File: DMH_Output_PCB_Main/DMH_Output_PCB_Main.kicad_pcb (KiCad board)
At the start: 2 copper layers, 49 x 175 mm, 91 parts, among them J0 Conn_01x01, J1 TRS_Jack_6.35mm_Sw, J100 IDC_02x05, J2 TRS_Jack_6.35mm_Sw, J200 IDC_02x05, J23 Conn_01x06, J24 Conn_01x02, J25 Conn_01x02, J26 Conn_01x06_PinHeader, J27 Conn_01x06_PinHeader, J28 Conn_01x06, J29 Conn_01x04_PinHeader, J3 TRS_Jack_6.35mm_Sw, J31 Conn_01x06_PinHeader, J35 Conn_01x04_PinHeader, J4 TRS_Jack_6.35mm_Sw, J5 TRS_Jack_6.35mm_Sw, J6 TRS_Jack_6.35mm_Sw, J7 TRS_Jack_6.35mm_Sw, J8 TRS_Jack_6.35mm_Sw, J9 TRS_Jack_6.35mm_Sw, U1 TL072, U11 TL074, U13 NE5532, U15 NE5532, U20 TL072, U8 TL074

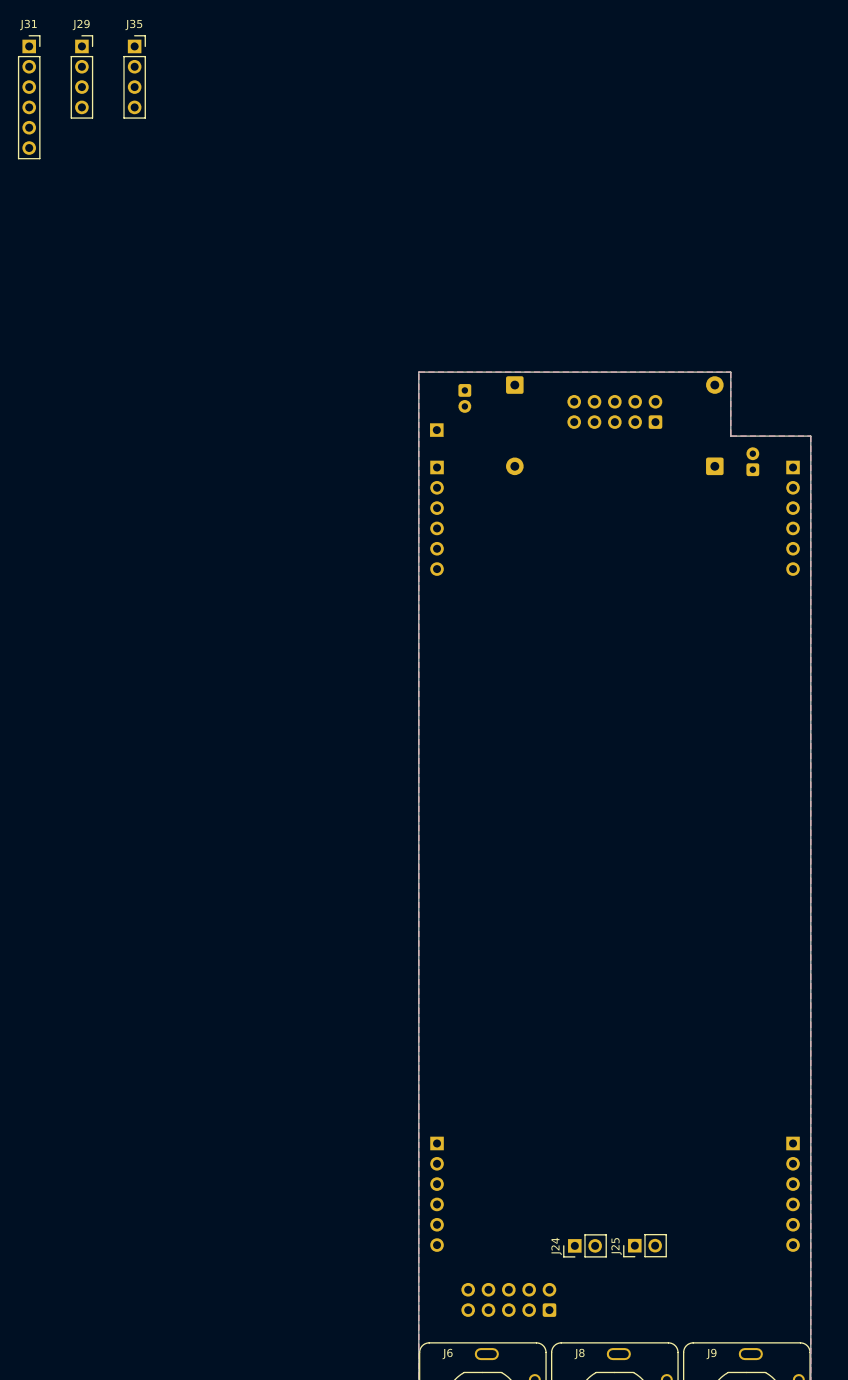
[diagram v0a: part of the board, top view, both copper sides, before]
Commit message: Placed pin sockets
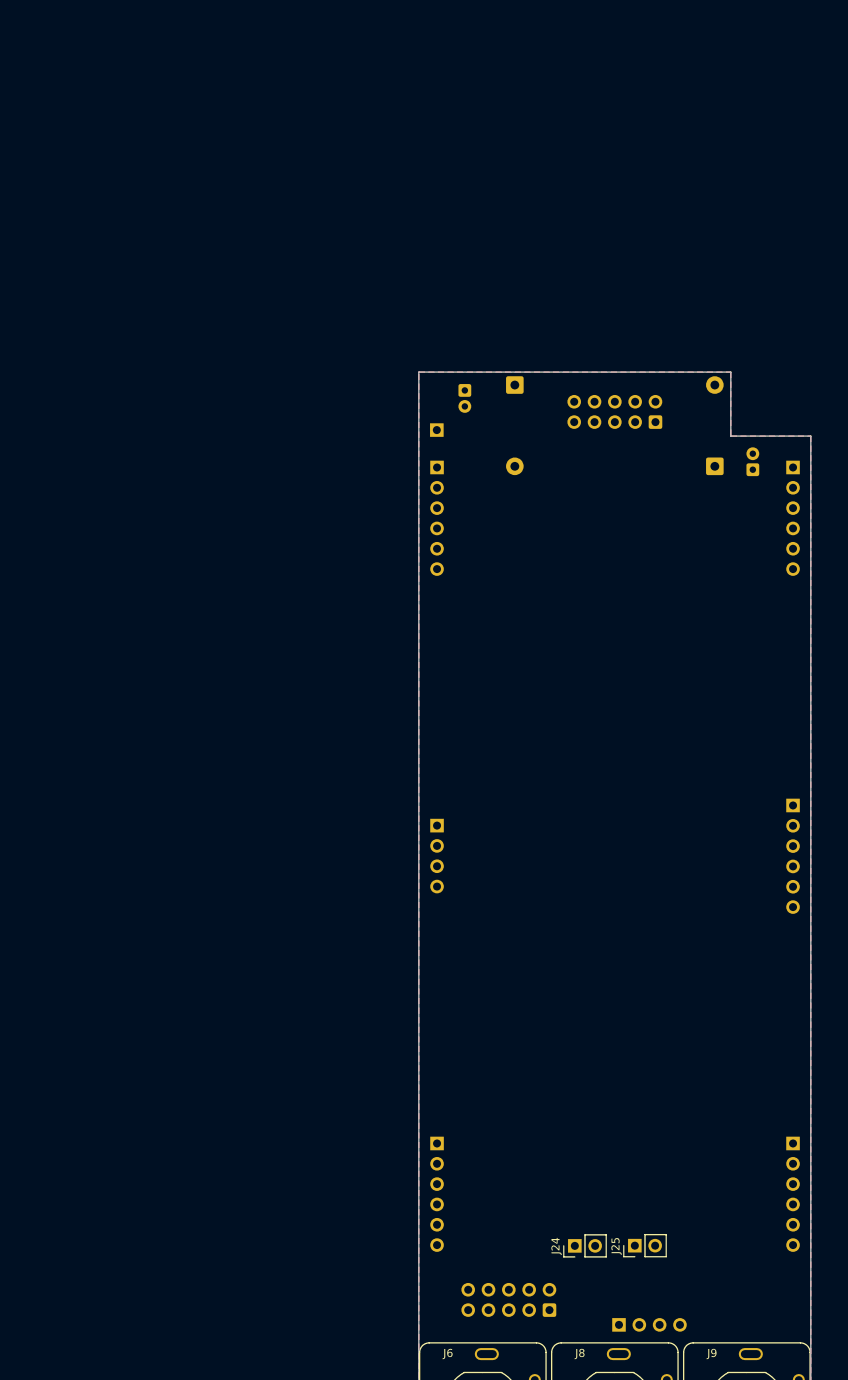
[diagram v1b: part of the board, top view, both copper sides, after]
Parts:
- J29, J31, J35: moved to B.Cu
- moved J35 170.9 mm to (75.5, 161.6), turned to -90 degrees
- moved J31 134.6 mm to (97.3, 96.7), turned to 180 degrees
- moved J29 107.0 mm to (52.8, 99.2), turned to 180 degrees
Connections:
- J29 pad 1: /Pre-Gain Stage/L_In_M -> /Pre-Gain Stage/R_In_M
- J29 pad 2: /Pre-Gain Stage/R_In_M -> /Pre-Gain Stage/L_In_M
- J31 pad 1: /Balanced Line Driver/L_Ch_OUT_M -> /Balanced Line Driver/R_Ch_OUT_M
- J31 pad 2: /Balanced Line Driver/R_Ch_OUT_M -> /Balanced Line Driver/L_Ch_OUT_M

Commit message: Main PCB comp placement in progress
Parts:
- C11, C12, C13, C14, C23, C24, C47, C48, C5, C50, C52, C54, C56, C57, C59, C6, C70, C72, C79, C80, D3, D33, D34, D4, D43, D44, D5, D6, R1, R2, R3, R30, R31, R32, R33, R44, R45, R46, R47, R48, R49, R5, R52, R53, R56, R57, R58, R59, R6, R8, R80, R81, R84, R86, R87, R89, R92, R94, R95, R97, U1, U11, U13, U15, U20, U8: moved to B.Cu
- moved C52 163.2 mm to (64.0, 60.2), turned to -90 degrees
- moved C50 159.0 mm to (86.0, 60.1), turned to -90 degrees
- moved C23 157.0 mm to (22.6, 115.6), turned to 180 degrees
- moved C24 156.8 mm to (22.4, 124.8), turned to 180 degrees
- moved C12 151.2 mm to (89.0, 63.6), turned to -90 degrees
- moved C11 149.9 mm to (89.0, 61.5), turned to 90 degrees
- moved R30 148.0 mm to (66.2, 55.8)
- moved R31 147.9 mm to (76.1, 55.8)
- moved R33 146.4 mm to (66.3, 69.6)
- moved C47 141.4 mm to (87.2, 105.3)
- moved U8 140.4 mm to (67.4, 58.9), turned to -90 degrees
- moved R32 138.8 mm to (76.2, 69.6)
- moved C48 133.2 mm to (87.2, 119.5)
- moved C54 132.4 mm to (57.5, 105.3)
- moved C56 129.4 mm to (57.5, 119.5)
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
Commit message: Main PCB comp placement in progress
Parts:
- moved C23 53.3 mm to (75.0, 125.8)
- moved C24 53.3 mm to (74.7, 135.0)
- moved J35 37.8 mm to (78.4, 199.3)
- moved R87 8.26 mm to (60.4, 133.9), turned to 0 degrees
- moved R86 7.61 mm to (60.4, 127.6), turned to 0 degrees
- moved R95 7.61 mm to (60.4, 143.5), turned to 0 degrees
- moved R94 7.61 mm to (60.4, 140.3), turned to 0 degrees
- moved R89 3.20 mm to (68.0, 130.7)
- moved D34 2.19 mm to (70.5, 116.7), turned to 90 degrees
- moved D33 0.51 mm to (67.3, 109.1)
- moved R97 0.10 mm to (68.0, 146.7)

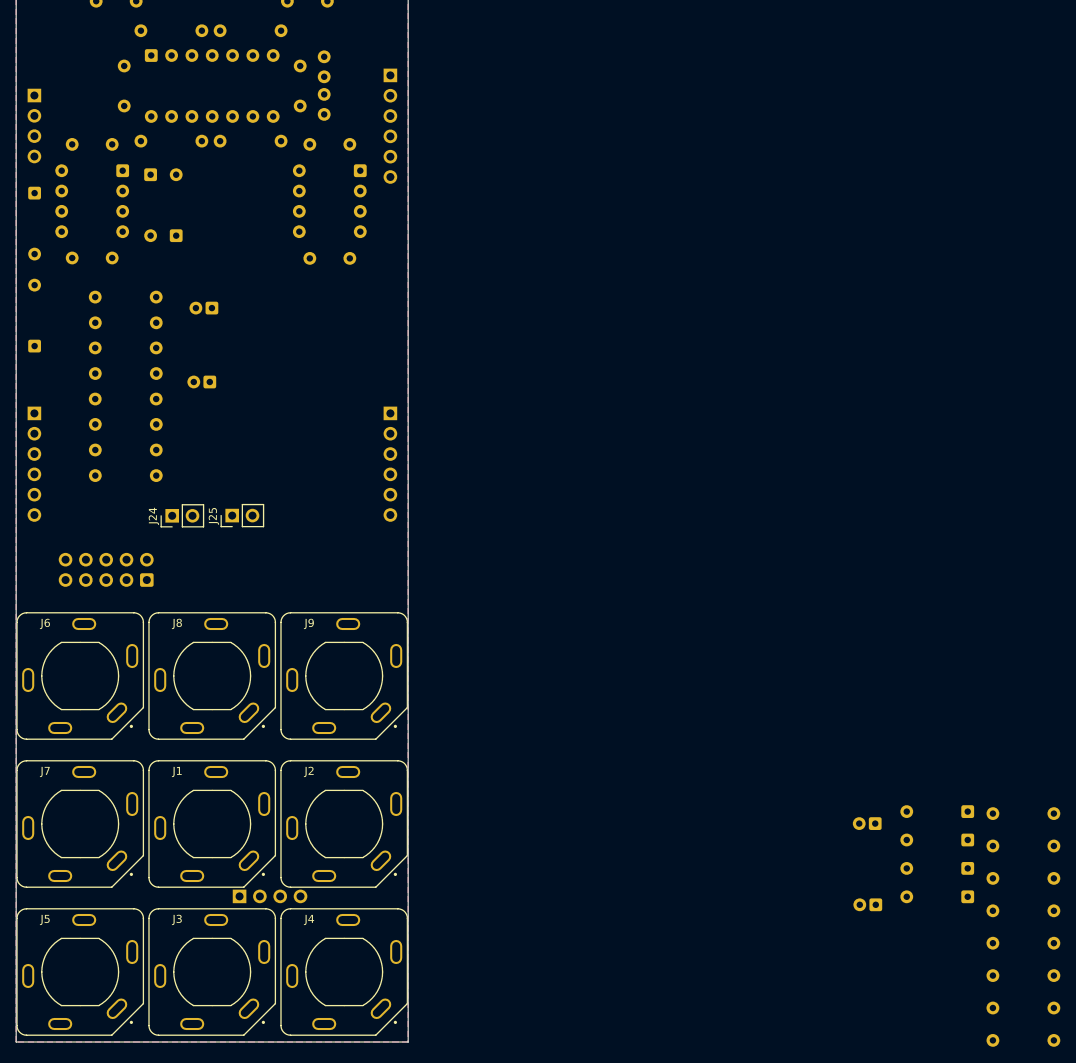
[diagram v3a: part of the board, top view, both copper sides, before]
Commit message: PCB Main comp placement done
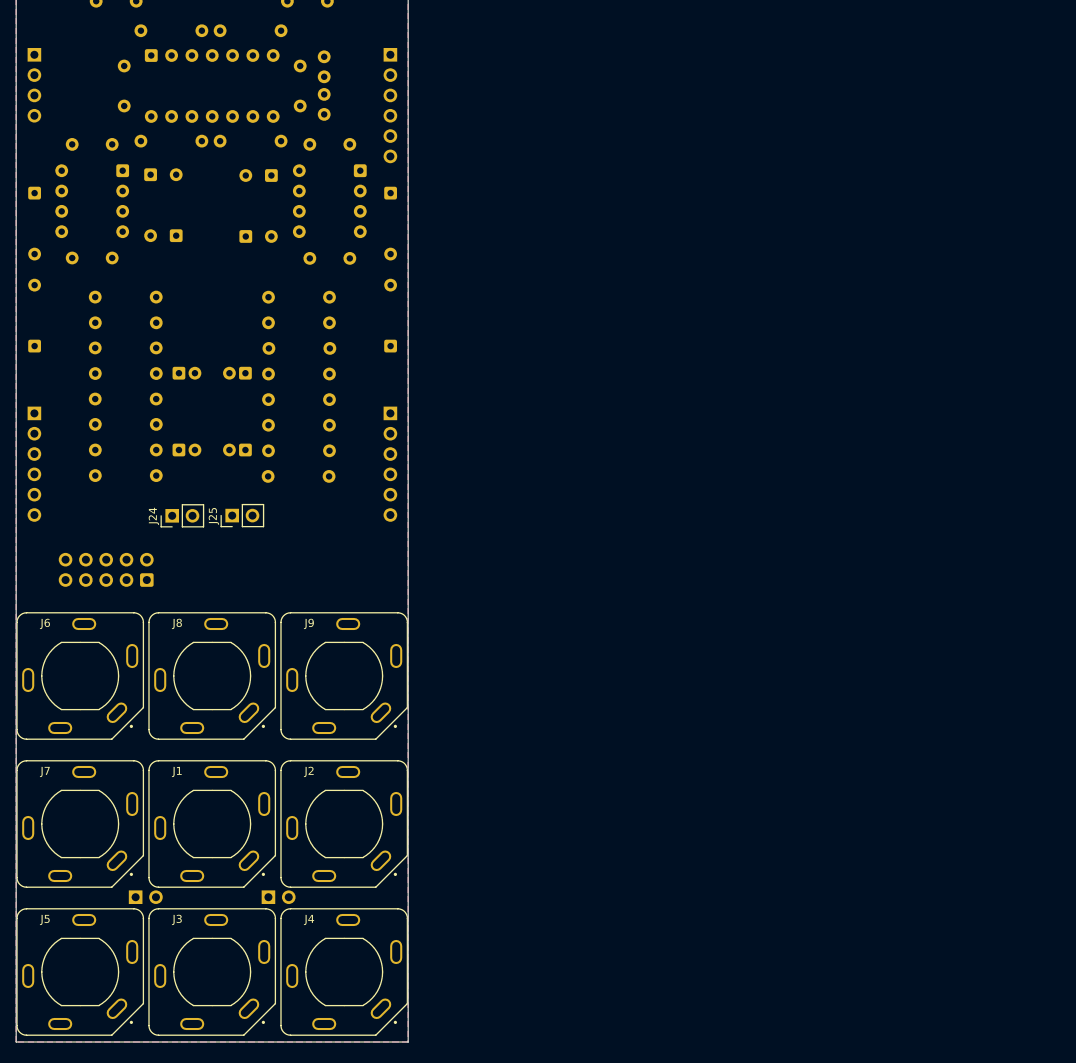
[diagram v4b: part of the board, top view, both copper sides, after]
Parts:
- added J36: Conn_01x02_PinHeader, Connector_PinSocket_2.54mm:PinSocket_1x02_P2.54mm_Vertical, B.Cu at (82.0, 199.4)
- J35: value Conn_01x04_PinHeader -> Conn_01x02_PinHeader; footprint Connector_PinSocket_2.54mm:PinSocket_1x04_P2.54mm_Vertical -> Connector_PinSocket_2.54mm:PinSocket_1x02_P2.54mm_Vertical
- R87, R95: value 100K -> 68K
- moved D5 122.8 mm to (82.4, 109.2), turned to -90 degrees
- moved D6 122.3 mm to (79.2, 116.8), turned to 90 degrees
- moved R80 120.3 mm to (89.7, 134.0)
- moved R81 116.8 mm to (89.7, 143.6)
- moved R3 114.1 mm to (89.7, 127.6)
- moved R1 114.1 mm to (82.1, 130.8), turned to 0 degrees
- moved R2 113.6 mm to (89.7, 124.4)
- moved R6 111.3 mm to (89.7, 140.4)
- moved R5 110.8 mm to (89.7, 137.2)
- moved R8 110.0 mm to (89.6, 146.8)
- moved D3 105.7 mm to (97.3, 111.4), turned to -90 degrees
- moved C6 97.2 mm to (79.2, 143.5)
- moved C5 96.8 mm to (79.2, 133.9)
- moved D4 95.0 mm to (97.3, 130.5), turned to 90 degrees
- moved J35 13.0 mm to (65.4, 199.4)
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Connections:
- J35 pad 2: /PreAmp/R_Ext_IN_M -> /Input Meter/L_Ext_Meter_M
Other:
- board text removed: "HP Amp"
- board text removed: "Input Meter"
- board text removed: "Output Meter"
- board text removed: "Volume"

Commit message: Main PCB routing in progress
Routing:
- net -12V: track 0.00 -> 182.9 mm
- net +12V: track 0.00 -> 170.0 mm
- net /Balanced Line Driver/L_Bal_OUT_N_M: track 0.00 -> 153.4 mm
- net /Balanced Line Driver/L_Bal_OUT_P_M: track 0.00 -> 144.3 mm
- net /Gain Trimmer/R_Gain_IN_M: track 0.00 -> 130.4 mm
- net /Headphone Amplifier/R_HP_OUT_M: track 0.00 -> 127.4 mm
- net /Gain Trimmer/L_Gain_IN_M: track 0.00 -> 117.2 mm
- net /Balanced Line Driver/R_Bal_OUT_P_M: track 0.00 -> 117.1 mm
- net /Balanced Line Driver/L_Ch_OUT_M: track 0.00 -> 108.9 mm
- net /Balanced Line Driver/R_Ch_OUT_M: track 0.00 -> 107.5 mm
- net /Balanced Line Driver/R_Bal_OUT_N_M: track 0.00 -> 104.0 mm
- net /Input Meter/R_Ext_Meter_M: track 0.00 -> 75.2 mm
- net /PreAmp/L_Ext_IN_M: track 0.00 -> 62.7 mm
- net Net-(D5-A): track 0.00 -> 52.0 mm
- net /PreAmp/R_Ext_IN_M: track 0.00 -> 51.5 mm
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
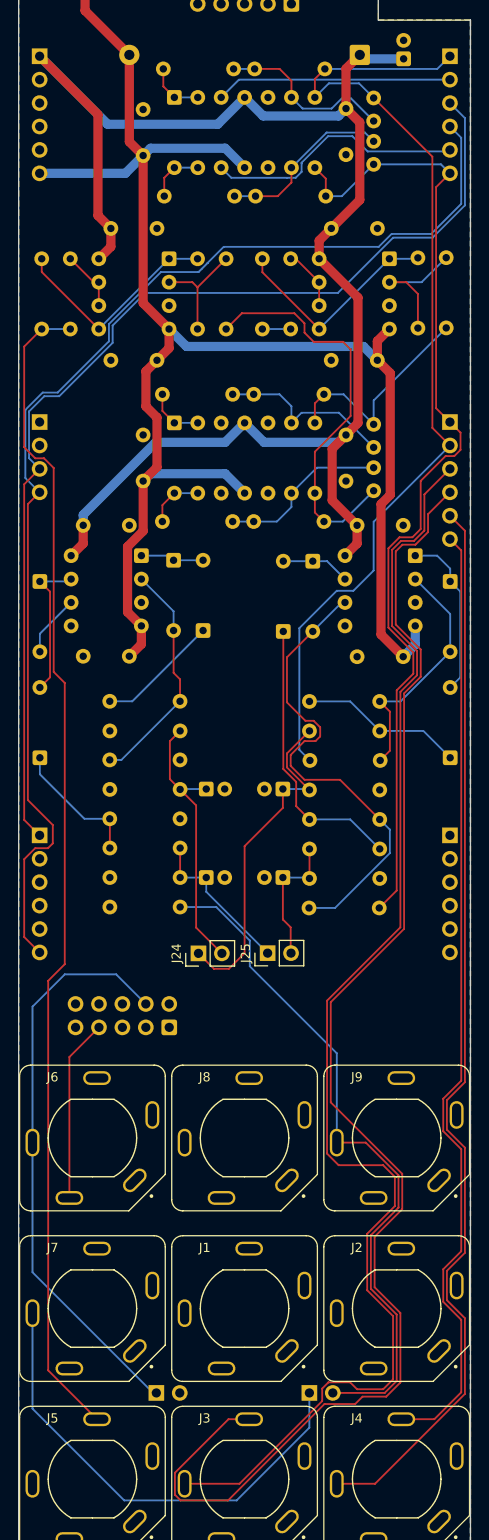
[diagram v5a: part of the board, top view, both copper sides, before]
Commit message: Main PCB routing done
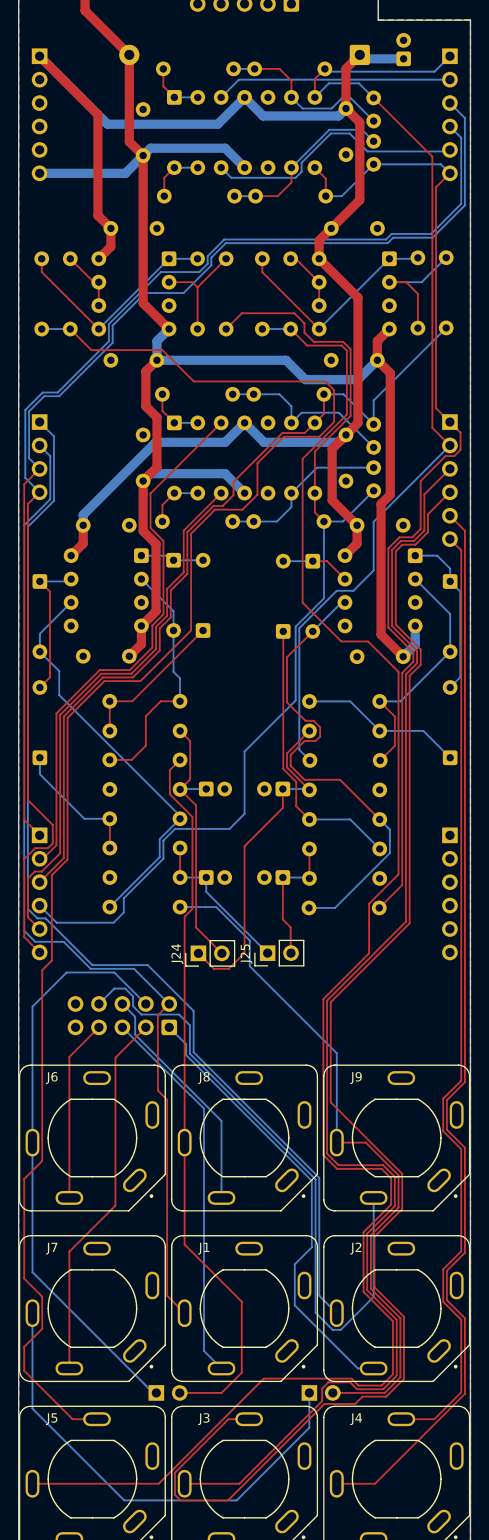
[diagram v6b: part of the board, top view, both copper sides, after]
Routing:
- net /Headphone Amplifier/L_HP_OUT_M: track 3.07 -> 185.6 mm
- net /Pre-Gain Stage/R_In_M: track 0.00 -> 116.4 mm
- net /Pre-Gain Stage/L_In_M: track 0.00 -> 108.5 mm
- net /Input Meter/L_Ext_Meter_M: track 0.00 -> 78.5 mm
- net Net-(J200-Pin_9): track 0.00 -> 68.9 mm
- net Net-(J27C-Pin_3): track 24.0 -> 90.0 mm
- net Net-(J27D-Pin_4): track 43.9 -> 109.4 mm
- net Net-(J27E-Pin_5): track 0.00 -> 58.8 mm
- net Net-(J27B-Pin_2): track 0.00 -> 58.7 mm
- net Net-(J2-2): track 0.00 -> 48.7 mm
- net /Headphone Amplifier/R_HP_OUT_M: track 127.4 -> 172.7 mm
- net Net-(J1-2): track 0.00 -> 41.5 mm
- net Net-(J200-Pin_2): track 0.00 -> 40.4 mm
- net Net-(D43-A): track 6.74 -> 43.9 mm
- net Net-(J200-Pin_8): track 0.00 -> 25.5 mm
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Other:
- board text added: "Mk1.0 May 2026"
